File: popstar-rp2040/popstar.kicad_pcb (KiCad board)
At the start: 2 copper layers, 284.7 x 94.2 mm, 182 parts, among them J1 JST SH 4-pin, J2 SWD, SW1 Boot, SW10 MX_SW_solder, SW11 MX_SW_solder, SW12 MX_SW_solder, SW13 MX_SW_solder, SW14 MX_SW_solder, SW15 MX_SW_solder, SW16 MX_SW_solder, SW17 MX_SW_solder, SW18 MX_SW_solder, SW19 MX_SW_solder, SW2 MX_SW_solder, SW20 MX_SW_solder, SW21 MX_SW_solder, SW22 MX_SW_solder, SW23 MX_SW_solder, SW24 MX_SW_solder, SW25 MX_SW_solder, SW26 MX_SW_solder, SW27 MX_SW_solder, SW28 MX_SW_solder, SW29 MX_SW_solder, SW3 MX_SW_solder, SW30 MX_SW_solder, SW31 MX_SW_solder, SW32 MX_SW_solder, SW33 MX_SW_solder, SW34 MX_SW_solder, SW35 MX_SW_solder, SW36 MX_SW_solder, SW37 MX_SW_solder, SW38 MX_SW_solder, SW39 MX_SW_solder, SW4 MX_SW_solder, SW40 MX_SW_solder, SW41 MX_SW_solder, SW42 MX_SW_solder, SW43 MX_SW_solder, SW44 MX_SW_solder, SW45 MX_SW_solder, SW46 MX_SW_solder, SW47 MX_SW_solder, SW48 MX_SW_solder, SW49 MX_SW_solder, SW5 MX_SW_solder, SW50 MX_SW_solder, SW51 MX_SW_solder, SW52 MX_SW_solder, SW53 MX_SW_solder, SW54 MX_SW_solder, SW55 MX_SW_solder, SW56 MX_SW_solder, SW57 MX_SW_solder, SW58 MX_SW_solder, SW59 MX_SW_solder, SW6 MX_SW_solder, SW60 MX_SW_solder, SW61 MX_SW_solder, SW62 MX_SW_solder, SW7 MX_SW_solder, SW8 MX_SW_solder, SW9 MX_SW_solder, U2 XC6206PxxxMR, U3 SRV05-4, U4 W25Q128JVS, U5 74AHCT1G125, U6 RP2040, Y1 12MHz

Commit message: Routed JST connector, ESD, voltage regulator, and more decoupling caps.
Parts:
- moved U3 0.54 mm to (61.7, 57.9)
- moved R2 0.31 mm to (62.5, 61.7)
- moved R3 0.31 mm to (60.9, 61.7)
- moved F1 0.25 mm to (51.7, 52.1)
- moved J1 0.13 mm to (57.0, 52.2)
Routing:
- net D_N: track 0.00 -> 19.2 mm
- net D_P: track 0.00 -> 17.9 mm
- net GND: track 43.4 -> 60.0 mm, vias 7 -> 14
- net +5V: track 0.00 -> 15.0 mm
- net /D_+: track 0.00 -> 6.29 mm
- net /D_-: track 0.00 -> 5.96 mm
- net +3V3: track 33.6 -> 39.2 mm
- net +1V1: track 4.76 -> 9.03 mm
- net VBUS: track 0.00 -> 3.35 mm

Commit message: Routed remainder of decoupling caps.
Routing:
- net +3V3: track 39.2 -> 46.9 mm
- net +1V1: track 9.03 -> 16.5 mm, vias 1 -> 2
- net GND: track 60.0 -> 63.3 mm, vias 14 -> 17
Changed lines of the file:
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@@
   (gr_arc (start 316.950016 99.604155) (mid 316.531156 100.8289) (end 315.450018 101.540649)
     (stroke (width 0.1) (type solid)) (layer "Edge.Cuts"))
+  (via (at 67.056 63.881) (size 0.8) (drill 0.4) (layers "F.Cu" "B.Cu") (net 1))
   (via (at 53.086 76.073) (size 0.8) (drill 0.4) (layers "F.Cu" "B.Cu") (net 1))
   (segment (start 56.676306 73.443915) (end 54.229 75.891223) (width 0.2) (layer "B.Cu") (net 1))
   (segment (start 60.689137 67.734028) (end 61.065654 67.357511) (width 0.2) (layer "B.Cu") (net 1))
   (segment (start 53.12525 76.03375) (end 53.086 76.073) (width 0.5) (layer "B.Cu") (net 1))
+  (segment (start 62.103351 69.148242) (end 65.913 65.338593) (width 0.2) (layer "B.Cu") (net 1))
   (segment (start 61.065654 67.357511) (end 61.065654 65.863654) (width 0.2) (layer "B.Cu") (net 1))
   (segment (start 60.689137 67.734028) (end 60.097165 68.326) (width 0.2) (layer "B.Cu") (net 1))
+  (segment (start 65.913 65.338593) (end 65.913 64.996) (width 0.2) (layer "B.Cu") (net 1))
   (segment (start 54.229 75.891223) (end 54.229 76.03375) (width 0.2) (layer "B.Cu") (net 1))
   (segment (start 54.229 76.03375) (end 53.12525 76.03375) (width 0.5) (layer "B.Cu") (net 1))
   (segment (start 61.065654 65.863654) (end 60.071 64.869) (width 0.2) (layer "B.Cu") (net 1))
+  (segment (start 67.056 64.037386) (end 67.056 63.881) (width 0.5) (layer "B.Cu") (net 1))
+  (segment (start 66.097386 64.996) (end 67.056 64.037386) (width 0.5) (layer "B.Cu") (net 1))
+  (segment (start 65.913 64.996) (end 66.097386 64.996) (width 0.5) (layer "B.Cu") (net 1))
   (via (at 56.769 53.594) (size 0.8) (drill 0.4) (layers "F.Cu" "B.Cu") (net 2))
   (via (at 54.229 78.105) (size 0.8) (drill 0.4) (layers "F.Cu" "B.Cu") (net 2))
   (via (at 56.261 62.738) (size 0.8) (drill 0.4) (layers "F.Cu" "B.Cu") (net 2))
+  (via (at 64.77 63.5) (size 0.8) (drill 0.4) (layers "F.Cu" "B.Cu") (net 2))
   (via (at 68.072 71.755) (size 0.8) (drill 0.4) (layers "F.Cu" "B.Cu") (net 2))
   (via (at 55.499 78.105) (size 0.8) (drill 0.4) (layers "F.Cu" "B.Cu") (net 2))
@@
   (via (at 54.864 86.487) (size 0.8) (drill 0.4) (layers "F.Cu" "B.Cu") (net 2))
   (via (at 57.531 62.738) (size 0.8) (drill 0.4) (layers "F.Cu" "B.Cu") (net 2))
+  (via (at 65.913 62.992) (size 0.8) (drill 0.4) (layers "F.Cu" "B.Cu") (net 2))
+  (via (at 63.5 64.008) (size 0.8) (drill 0.4) (layers "F.Cu" "B.Cu") (net 2))
   (via (at 63.754 79.375) (size 0.8) (drill 0.4) (layers "F.Cu" "B.Cu") (net 2))
   (via (at 64.135 55.372) (size 0.8) (drill 0.4) (layers "F.Cu" "B.Cu") (net 2))
@@
   (via (at 58.801 62.738) (size 0.8) (drill 0.4) (layers "F.Cu" "B.Cu") (net 2))
   (via (at 52.451 68.199) (size 0.8) (drill 0.4) (layers "F.Cu" "B.Cu") (net 2))
+  (segment (start 63.5 65.179) (end 63.5 64.008) (width 0.5) (layer "B.Cu") (net 2))
   (segment (start 56.13775 61.595) (end 56.0425 61.69025) (width 0.5) (layer "B.Cu") (net 2))
   (segment (start 57.061 75.321963) (end 57.061 77.343) (width 0.2) (layer "B.Cu") (net 2))
@@
   (segment (start 66.421 71.727) (end 68.044 71.727) (width 0.5) (layer "B.Cu") (net 2))
   (segment (start 62.611 79.347) (end 63.726 79.347) (width 0.5) (layer "B.Cu") (net 2))
+  (segment (start 64.7065 63.5635) (end 64.77 63.5) (width 0.5) (layer "B.Cu") (net 2))
   (segment (start 68.044 71.727) (end 68.072 71.755) (width 0.2) (layer "B.Cu") (net 2))
   (segment (start 56.5125 60.0655) (end 56.5125 60.9575) (width 0.5) (layer "B.Cu") (net 2))
@@
   (segment (start 54.229 76.99375) (end 55.499 76.99375) (width 0.5) (layer "B.Cu") (net 2))
   (segment (start 57.178843 79.092157) (end 57.785 79.698314) (width 0.2) (layer "B.Cu") (net 2))
+  (segment (start 65.913 64.036) (end 65.913 62.992) (width 0.5) (layer "B.Cu") (net 2))
   (segment (start 52.606 68.354) (end 52.451 68.199) (width 0.2) (layer "B.Cu") (net 2))
   (segment (start 57.061 77.343) (end 57.061 77.450314) (width 0.2) (layer "B.Cu") (net 2))
@@
   (segment (start 57.56275 62.76975) (end 57.531 62.738) (width 0.5) (layer "B.Cu") (net 2))
   (segment (start 52.3875 58.7375) (end 52.451 58.801) (width 0.5) (layer "B.Cu") (net 2))
+  (segment (start 64.7065 64.6075) (end 64.7065 63.5635) (width 0.5) (layer "B.Cu") (net 2))
   (segment (start 55.0825 63.874886) (end 55.0825 61.69025) (width 0.5) (layer "B.Cu") (net 3))
   (segment (start 64.389 72.618297) (end 64.795703 72.618297) (width 0.2) (layer "B.Cu") (net 3))
+  (segment (start 61.537665 68.582556) (end 63.5 66.620221) (width 0.2) (layer "B.Cu") (net 3))
   (segment (start 53.744411 69.337411) (end 53.721 69.314) (width 0.2) (layer "B.Cu") (net 3))
   (segment (start 56.959149 73.726758) (end 55.499 75.186909) (width 0.2) (layer "B.Cu") (net 3))
@@
   (segment (start 62.611 75.931463) (end 62.611 78.387) (width 0.2) (layer "B.Cu") (net 3))
   (segment (start 55.499 75.186909) (end 55.499 76.03375) (width 0.2) (layer "B.Cu") (net 3))
+  (segment (start 63.5 66.620221) (end 63.5 66.139) (width 0.2) (layer "B.Cu") (net 3))
   (segment (start 56.959149 73.726758) (end 57.531 73.154905) (width 0.2) (layer "B.Cu") (net 3))
   (segment (start 56.016946 69.337411) (end 53.744411 69.337411) (width 0.2) (layer "B.Cu") (net 3))
+  (segment (start 64.7065 65.979407) (end 64.7065 65.5675) (width 0.2) (layer "B.Cu") (net 3))
   (segment (start 76.0255 70.767) (end 77.41875 69.37375) (width 0.5) (layer "B.Cu") (net 3))
   (segment (start 53.721 69.314) (end 53.693 69.342) (width 0.2) (layer "B.Cu") (net 3))
@@
   (segment (start 61.254823 74.575286) (end 62.611 75.931463) (width 0.2) (layer "B.Cu") (net 3))
   (segment (start 63.800407 72.029702) (end 64.389 72.618297) (width 0.2) (layer "B.Cu") (net 3))
+  (segment (start 61.820508 68.865399) (end 64.7065 65.979407) (width 0.2) (layer "B.Cu") (net 3))
   (segment (start 65.659 71.12) (end 66.012 70.767) (width 0.2) (layer "B.Cu") (net 3))
   (segment (start 56.393464 69.713927) (end 57.023 70.343465) (width 0.2) (layer "B.Cu") (net 3))

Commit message: Routed flash, boot
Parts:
- moved C7 0.59 mm to (64.1, 65.0)
- moved C11 0.52 mm to (63.0, 65.5)
- moved C1 0.52 mm to (65.4, 64.4)
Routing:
- net SD3: track 0.00 -> 24.7 mm
- net QSPI_CLK: track 0.00 -> 22.2 mm
- net CS: track 0.00 -> 19.8 mm
- net SD0: track 0.00 -> 18.0 mm
- net SD2: track 0.00 -> 8.41 mm
- net SD1: track 0.00 -> 7.72 mm
- net GND: track 63.3 -> 69.4 mm, vias 17 -> 20
- net /~{USB_BOOT}: track 0.00 -> 2.46 mm
- net +1V1: track 16.5 -> 14.7 mm, vias 2 -> 1

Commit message: Properly connected diodes to switches in the schematic
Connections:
- D15 pad 1: unconnected-(D15-K-Pad1) -> ROW0
- D16 pad 1: unconnected-(D16-K-Pad1) -> ROW0
- D17 pad 1: unconnected-(D17-K-Pad1) -> ROW0
- D18 pad 1: unconnected-(D18-K-Pad1) -> ROW0
- D19 pad 1: unconnected-(D19-K-Pad1) -> ROW0
- D20 pad 1: unconnected-(D20-K-Pad1) -> ROW0
- D21 pad 1: unconnected-(D21-K-Pad1) -> ROW0
- D22 pad 1: unconnected-(D22-K-Pad1) -> ROW0
- D23 pad 1: unconnected-(D23-K-Pad1) -> ROW0
- D24 pad 1: unconnected-(D24-K-Pad1) -> ROW0
- D29 pad 1: unconnected-(D29-K-Pad1) -> ROW1
- D30 pad 1: unconnected-(D30-K-Pad1) -> ROW1
- D31 pad 1: unconnected-(D31-K-Pad1) -> ROW1
- D32 pad 1: unconnected-(D32-K-Pad1) -> ROW1
- D33 pad 1: unconnected-(D33-K-Pad1) -> ROW1
- D34 pad 1: unconnected-(D34-K-Pad1) -> ROW1
- D35 pad 1: unconnected-(D35-K-Pad1) -> ROW1
- D36 pad 1: unconnected-(D36-K-Pad1) -> ROW1
- D37 pad 1: unconnected-(D37-K-Pad1) -> ROW1
- D38 pad 1: unconnected-(D38-K-Pad1) -> ROW1
- D42 pad 1: unconnected-(D42-K-Pad1) -> ROW2
- D43 pad 1: unconnected-(D43-K-Pad1) -> ROW2
- D44 pad 1: unconnected-(D44-K-Pad1) -> ROW2
- D45 pad 1: unconnected-(D45-K-Pad1) -> ROW2
- D46 pad 1: unconnected-(D46-K-Pad1) -> ROW2
- D47 pad 1: unconnected-(D47-K-Pad1) -> ROW2
- D48 pad 1: unconnected-(D48-K-Pad1) -> ROW2
- D49 pad 1: unconnected-(D49-K-Pad1) -> ROW2
- D50 pad 1: unconnected-(D50-K-Pad1) -> ROW2
- D51 pad 1: unconnected-(D51-K-Pad1) -> ROW2
- D55 pad 1: unconnected-(D55-K-Pad1) -> ROW3
- D56 pad 1: unconnected-(D56-K-Pad1) -> ROW3
- D57 pad 1: unconnected-(D57-K-Pad1) -> ROW3
- D58 pad 1: unconnected-(D58-K-Pad1) -> ROW3
- D59 pad 1: unconnected-(D59-K-Pad1) -> ROW3
- D60 pad 1: unconnected-(D60-K-Pad1) -> ROW3
- D61 pad 1: unconnected-(D61-K-Pad1) -> ROW3
- D62 pad 1: unconnected-(D62-K-Pad1) -> ROW3
- D63 pad 1: unconnected-(D63-K-Pad1) -> ROW3
- D64 pad 1: unconnected-(D64-K-Pad1) -> ROW3
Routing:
- net ROW2: track 8.07 -> 48.0 mm, vias 0 -> 2
- net Net-(D41-A): track 0.00 -> 8.05 mm
- net COL05: track 7.71 -> 0.00 mm
- net COL04: track 7.53 -> 0.00 mm
- net COL02: track 7.16 -> 0.00 mm
- net COL03: track 6.84 -> 0.00 mm
- net COL06: track 4.63 -> 0.00 mm
- net COL07: track 4.30 -> 0.00 mm
- net COL08: track 3.60 -> 0.00 mm
- net COL10: track 5.21 -> 3.32 mm
- net COL11: track 5.90 -> 4.69 mm
- net COL12: track 6.59 -> 6.08 mm

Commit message: Finished routing rows, cleaned up existing traces. Switched row0 and col0 for cleaner routing.
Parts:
- moved D71 2.55 mm to (303.2, 47.0), turned to 90 degrees
- moved R1 1.25 mm to (49.0, 67.0)
- moved J2 1.03 mm to (39.9, 69.3)
- moved C4 1.02 mm to (57.2, 64.0)
- moved C6 0.92 mm to (58.4, 64.0)
- moved C10 0.89 mm to (59.6, 64.0)
- moved C2 0.80 mm to (60.8, 64.0)
- moved D28 0.71 mm to (78.5, 60.3)
- moved SW18 0.70 mm to (70.5, 60.3)
- moved SW17 0.70 mm to (46.7, 60.3)
- moved R2 0.44 mm to (62.5, 61.2)
- moved R3 0.44 mm to (60.9, 61.2)
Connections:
- U6 pad 38: ROW0 -> COL01
- U6 pad 39: COL01 -> ROW0
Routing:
- net ROW4: track 0.00 -> 356.8 mm
- net ROW3: track 0.00 -> 314.6 mm
- net ROW1: track 0.00 -> 312.5 mm
- net ROW0: track 0.00 -> 278.9 mm
- net ROW2: track 48.0 -> 298.8 mm
- net COL01: track 0.00 -> 71.1 mm
- net Net-(D26-A): track 0.00 -> 29.2 mm
- net COL00: track 0.00 -> 22.2 mm
- net Net-(D72-A): track 0.00 -> 18.8 mm
- net Net-(D71-A): track 0.00 -> 16.6 mm
- net Net-(D65-A): track 0.00 -> 15.4 mm
- net Net-(D52-A): track 0.00 -> 9.96 mm
- net Net-(D40-A): track 0.00 -> 8.98 mm
- net Net-(D51-A): track 0.00 -> 8.05 mm
- net Net-(D38-A): track 0.00 -> 8.05 mm
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
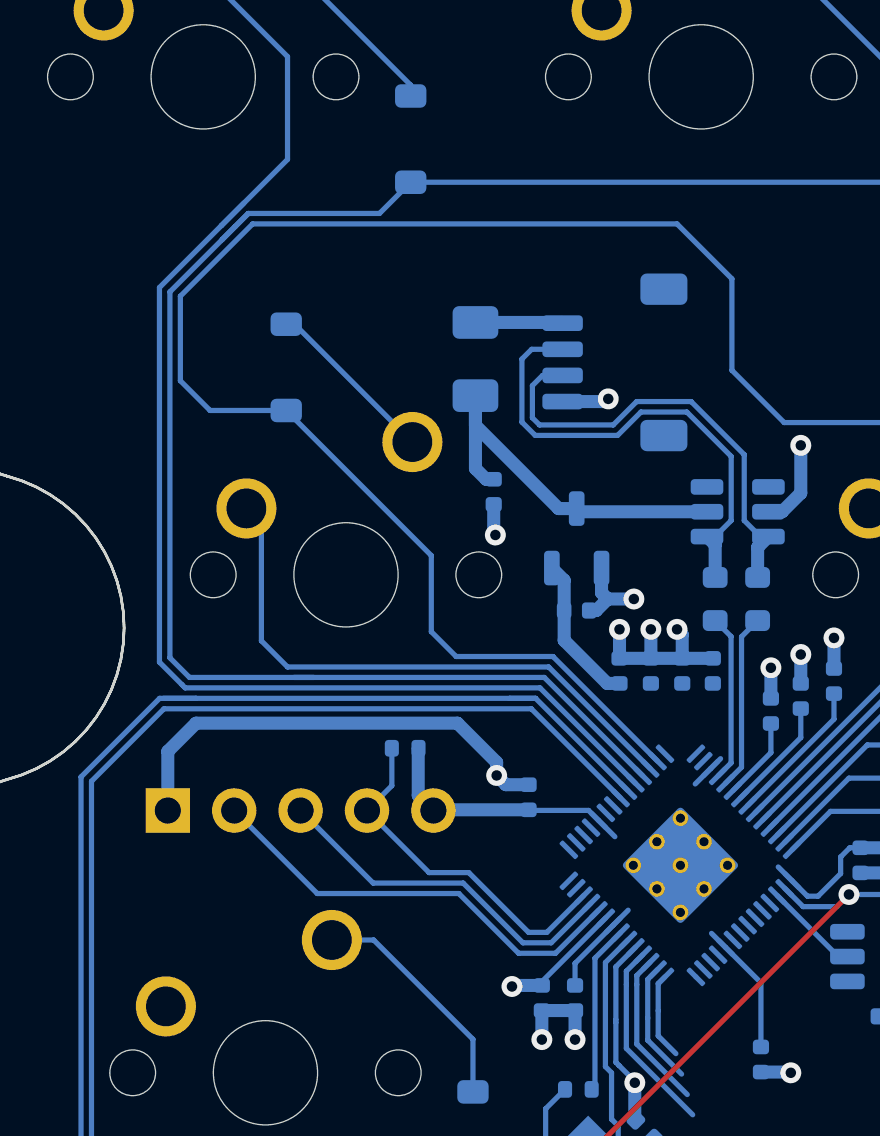
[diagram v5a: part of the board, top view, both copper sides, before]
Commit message: Further removed some duplicate, unconnected traces
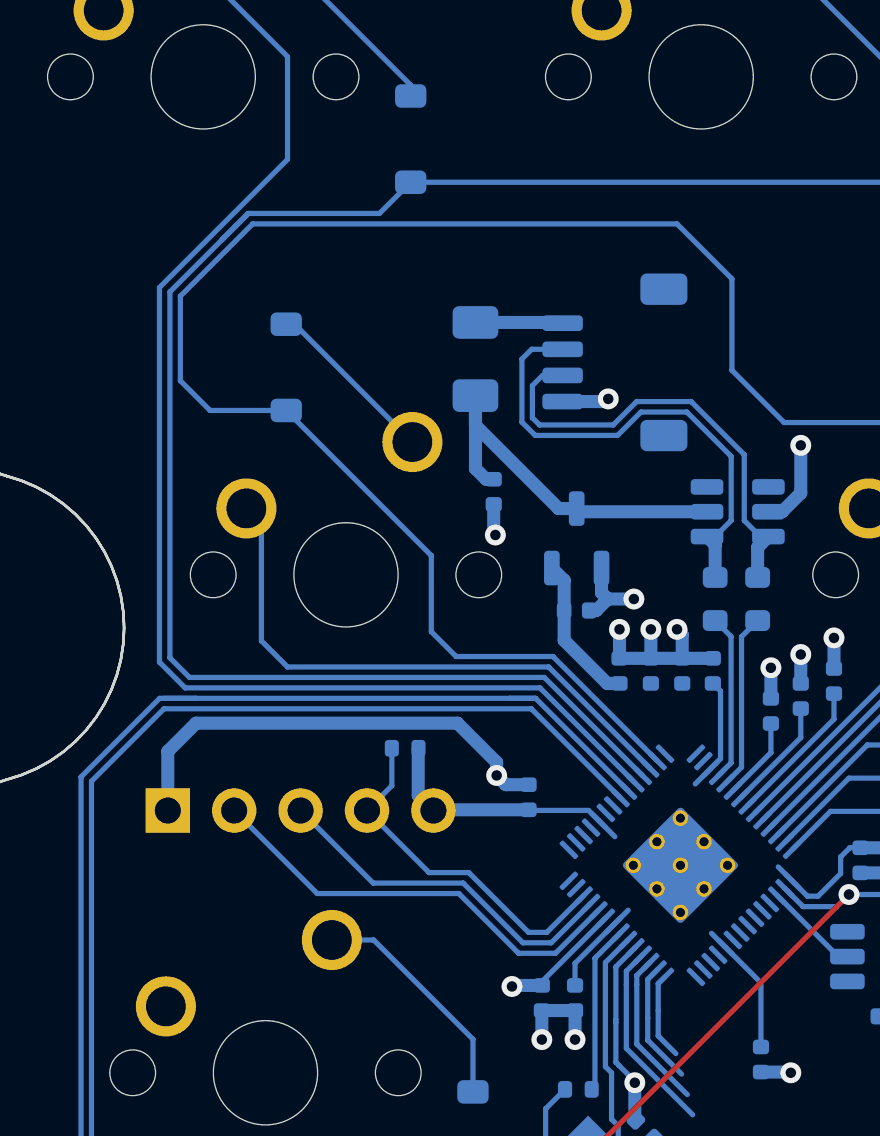
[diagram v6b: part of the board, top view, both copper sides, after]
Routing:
- net +1V1: track 11.8 -> 14.8 mm
- net COL01: track 71.1 -> 69.9 mm
- net ROW0: track 278.9 -> 278.1 mm
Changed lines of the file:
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@@
     (stroke (width 0.1) (type solid)) (layer "Edge.Cuts"))
   (via (at 53.086 76.073) (size 0.8) (drill 0.4) (layers "F.Cu" "B.Cu") (net 1))
+  (segment (start 61.065654 64.775654) (end 60.77 64.48) (width 0.2) (layer "B.Cu") (net 1))
   (segment (start 62.103351 69.148242) (end 65.405 65.846593) (width 0.2) (layer "B.Cu") (net 1))
   (segment (start 56.676306 73.443915) (end 54.229 75.891223) (width 0.2) (layer "B.Cu") (net 1))
   (segment (start 65.405 65.846593) (end 65.405 64.869) (width 0.2) (layer "B.Cu") (net 1))
+  (segment (start 53.12525 76.03375) (end 53.086 76.073) (width 0.5) (layer "B.Cu") (net 1))
   (segment (start 60.689137 67.734028) (end 61.065654 67.357511) (width 0.2) (layer "B.Cu") (net 1))
-  (segment (start 53.12525 76.03375) (end 53.086 76.073) (width 0.5) (layer "B.Cu") (net 1))
   (segment (start 60.689137 67.734028) (end 60.097165 68.326) (width 0.2) (layer "B.Cu") (net 1))
   (segment (start 54.229 75.891223) (end 54.229 76.03375) (width 0.2) (layer "B.Cu") (net 1))
   (segment (start 54.229 76.03375) (end 53.12525 76.03375) (width 0.5) (layer "B.Cu") (net 1))
+  (segment (start 61.065654 67.357511) (end 61.065654 64.775654) (width 0.2) (layer "B.Cu") (net 1))
   (via (at 56.769 53.594) (size 0.8) (drill 0.4) (layers "F.Cu" "B.Cu") (net 2))
   (via (at 62.992 63.881) (size 0.8) (drill 0.4) (layers "F.Cu" "B.Cu") (net 2))
@@
   (segment (start 61.537665 68.582556) (end 62.992 67.128221) (width 0.2) (layer "B.Cu") (net 3))
   (segment (start 49.5 66.97075) (end 49.51 66.96075) (width 0.5) (layer "B.Cu") (net 3))
-  (segment (start 53.744411 69.337411) (end 53.721 69.314) (width 0.2) (layer "B.Cu") (net 3))
   (segment (start 56.959149 73.726758) (end 55.499 75.186909) (width 0.2) (layer "B.Cu") (net 3))
   (segment (start 65.659 71.755) (end 65.659 71.12) (width 0.2) (layer "B.Cu") (net 3))
@@
   (segment (start 106.3625 45.30625) (end 125.4125 45.30625) (width 0.2) (layer "B.Cu") (net 20))
   (segment (start 87.3125 45.30625) (end 106.3625 45.30625) (width 0.2) (layer "B.Cu") (net 20))
-  (segment (start 54.323649 64.25) (end 40.75 64.25) (width 0.2) (layer "B.Cu") (net 20))
-  (segment (start 58.09052 68.016871) (end 54.323649 64.25) (width 0.2) (layer "B.Cu") (net 20))
   (segment (start 42 47.5) (end 43 46.5) (width 0.2) (layer "B.Cu") (net 20))
   (segment (start 43 46.5) (end 48.01875 46.5) (width 0.2) (layer "B.Cu") (net 20))
@@
   (segment (start 125.4125 45.30625) (end 144.4625 45.30625) (width 0.2) (layer "B.Cu") (net 20))
   (segment (start 42.5 47) (end 43 46.5) (width 0.2) (layer "B.Cu") (net 20))
+  (segment (start 58.09052 68.016871) (end 54.323649 64.25) (width 0.2) (layer "B.Cu") (net 20))
   (segment (start 49.2125 45.30625) (end 68.2625 45.30625) (width 0.2) (layer "B.Cu") (net 20))
+  (segment (start 40.75 64.25) (end 40 63.5) (width 0.2) (layer "B.Cu") (net 20))
   (segment (start 182.5625 45.30625) (end 201.6125 45.30625) (width 0.2) (layer "B.Cu") (net 20))
+  (segment (start 54.323649 64.25) (end 40.75 64.25) (width 0.2) (layer "B.Cu") (net 20))
   (segment (start 68.2625 45.30625) (end 87.3125 45.30625) (width 0.2) (layer "B.Cu") (net 20))
   (segment (start 42 47.5) (end 42.5 47) (width 0.2) (layer "B.Cu") (net 20))
@@
   (segment (start 163.5125 45.30625) (end 182.5625 45.30625) (width 0.2) (layer "B.Cu") (net 20))
   (segment (start 220.6625 45.30625) (end 239.7125 45.30625) (width 0.2) (layer "B.Cu") (net 20))
-  (segment (start 40.75 64.25) (end 40 63.5) (width 0.2) (layer "B.Cu") (net 20))
   (segment (start 201.6125 45.30625) (end 220.6625 45.30625) (width 0.2) (layer "B.Cu") (net 20))
-  (segment (start 45.5 64.25) (end 44.75 64.25) (width 0.2) (layer "B.Cu") (net 20))
+  (segment (start 40 63.5) (end 40 49.5) (width 0.2) (layer "B.Cu") (net 20))
+  (segment (start 277.8125 45.30625) (end 280.9875 45.30625) (width 0.2) (layer "B.Cu") (net 20))
   (segment (start 40 49.5) (end 42 47.5) (width 0.2) (layer "B.Cu") (net 20))
-  (segment (start 277.8125 45.30625) (end 280.9875 45.30625) (width 0.2) (layer "B.Cu") (net 20))
   (segment (start 144.4625 45.30625) (end 163.5125 45.30625) (width 0.2) (layer "B.Cu") (net 20))
-  (segment (start 40 63.5) (end 40 49.5) (width 0.2) (layer "B.Cu") (net 20))
   (segment (start 48.01875 46.5) (end 49.2125 45.30625) (width 0.2) (layer "B.Cu") (net 20))
   (segment (start 49.2125 42.00625) (end 49.2125 41.5925) (width 0.2) (layer "B.Cu") (net 21))
@@
   (segment (start 43.5 62.85) (end 43.5 58.3585) (width 0.2) (layer "B.Cu") (net 96))
   (segment (start 44.5 63.85) (end 43.5 62.85) (width 0.2) (layer "B.Cu") (net 96))
-  (segment (start 40.584314 64.65) (end 40.467157 64.532843) (width 0.2) (layer "B.Cu") (net 97))
+  (segment (start 41 37) (end 41 35.5) (width 0.2) (layer "B.Cu") (net 97))
+  (segment (start 41 35.5) (end 42.5 34) (width 0.2) (layer "B.Cu") (net 97))
+  (segment (start 42.5 34) (end 51.78 34) (width 0.2) (layer "B.Cu") (net 97))
+  (segment (start 51.78 34) (end 56.515 38.735) (width 0.2) (layer "B.Cu") (net 97))
+  (segment (start 39.6 49.334314) (end 44.5 44.434314) (width 0.2) (layer "B.Cu") (net 97))
+  (segment (start 44.5 44.434314) (end 44.5 40.5) (width 0.2) (layer "B.Cu") (net 97))
+  (segment (start 57.807677 68.299714) (end 54.157964 64.65) (width 0.2) (layer "B.Cu") (net 97))
   (segment (start 39.6 63.665685) (end 39.6 49.334314) (width 0.2) (layer "B.Cu") (net 97))
-  (segment (start 41 35.5) (end 42.5 34) (width 0.2) (layer "B.Cu") (net 97))
-  (segment (start 41.967157 46.967157) (end 42.834315 46.1) (width 0.2) (layer "B.Cu") (net 97))
-  (segment (start 42.5 34) (end 51.78 34) (width 0.2) (layer "B.Cu") (net 97))
+  (segment (start 44.5 40.5) (end 41 37) (width 0.2) (layer "B.Cu") (net 97))
   (segment (start 54.157964 64.65) (end 40.584314 64.65) (width 0.2) (layer "B.Cu") (net 97))
-  (segment (start 41 37) (end 41 35.5) (width 0.2) (layer "B.Cu") (net 97))
-  (segment (start 57.807677 68.299714) (end 54.157964 64.65) (width 0.2) (layer "B.Cu") (net 97))
-  (segment (start 44.5 40.5) (end 41 37) (width 0.2) (layer "B.Cu") (net 97))
-  (segment (start 51.78 34) (end 56.515 38.735) (width 0.2) (layer "B.Cu") (net 97))
-  (segment (start 40.467157 64.532843) (end 39.6 63.665685) (width 0.2) (layer "B.Cu") (net 97))
-  (segment (start 44.5 44.434314) (end 44.5 40.5) (width 0.2) (layer "B.Cu") (net 97))
-  (segment (start 39.6 49.334314) (end 41.967157 46.967157) (width 0.2) (layer "B.Cu") (net 97))
-  (segment (start 41.967157 46.967157) (end 44.5 44.434314) (width 0.2) (layer "B.Cu") (net 97))
-  (segment (start 60.123452 75.706657) (end 60.123453 75.706657) (width 0.2) (layer "B.Cu") (net 105))
+  (segment (start 40.584314 64.65) (end 39.6 63.665685) (width 0.2) (layer "B.Cu") (net 97))
   (segment (start 58.679689 77) (end 58.679689 77.963681) (width 0.2) (layer "B.Cu") (net 106))
   (segment (start 58.679689 75.966016) (end 58.679689 77) (width 0.2) (layer "B.Cu") (net 106))

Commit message: Fixed all DRC errors unrelated to split BS
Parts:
- moved SW18 0.70 mm to (69.8, 60.3)
- moved SW17 0.70 mm to (46.0, 60.3)
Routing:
- net COL00: track 22.2 -> 113.3 mm
- net COL01: track 69.9 -> 94.6 mm
- net ROW0: track 278.1 -> 277.5 mm
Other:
- outline, holes or cut-outs redrawn
